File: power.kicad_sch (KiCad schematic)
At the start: 13 parts, among them J601 CONN_12V, J602 Screw_Terminal_01x02, Q601 DMP3037LSS, SW601 PWR_SW, U601 LM2576S-3.3

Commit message: Power switch footprint.
This is the last footprint!
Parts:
- SW601: footprint (none) -> marco-ram-board:SW_CuK_L101xxxMS02x_SPST_Straight; Part (none) -> 611-L101011MS02Q
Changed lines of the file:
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@@
     (property "Reference" "SW601" (id 0) (at 109.22 67.0392 0))
     (property "Value" "PWR_SW" (id 1) (at 109.22 69.5761 0))
-    (property "Footprint" "" (id 2) (at 109.22 72.39 0)
+    (property "Footprint" "marco-ram-board:SW_CuK_L101xxxMS02x_SPST_Straight" (id 2) (at 109.22 72.39 0)
       (effects (font (size 1.27 1.27)) hide)
     )
-    (property "Datasheet" "~" (id 3) (at 109.22 72.39 0)
+    (property "Datasheet" "https://www.ckswitches.com/media/1423/l.pdf" (id 3) (at 109.22 72.39 0)
       (effects (font (size 1.27 1.27)) hide)
     )
+    (property "Part" "611-L101011MS02Q" (id 4) (at 109.22 72.39 0)
+      (effects (font (size 1.27 1.27)) hide)
+    )

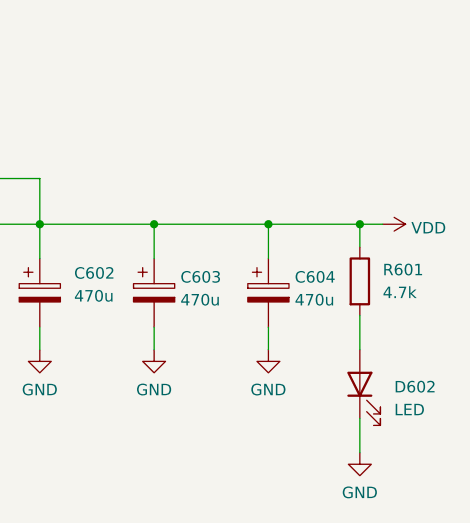
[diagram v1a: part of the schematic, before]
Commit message: Fix led current limiting resistor values.
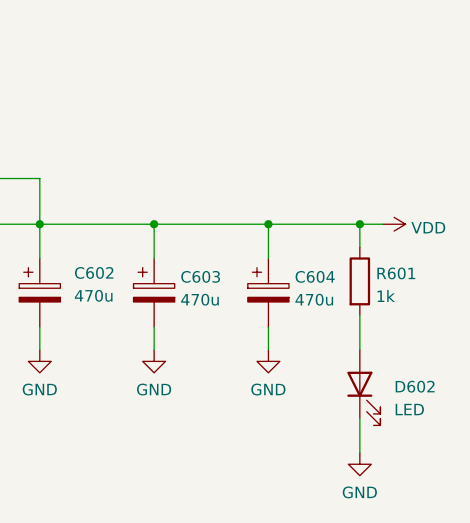
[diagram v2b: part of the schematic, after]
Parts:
- R601: value 4.7k -> 1k
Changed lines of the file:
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@@
   (symbol (lib_id "Device:R") (at 229.87 83.82 0) (unit 1)
     (in_bom yes) (on_board yes) (fields_autoplaced)
-    (property "Reference" "R601" (id 0) (at 232.41 82.5499 0)
+    (property "Reference" "R601" (id 0) (at 231.648 82.9853 0)
       (effects (font (size 1.27 1.27)) (justify left))
     )
-    (property "Value" "4.7k" (id 1) (at 232.41 85.0899 0)
+    (property "Value" "1k" (id 1) (at 231.648 85.5222 0)
       (effects (font (size 1.27 1.27)) (justify left))
     )

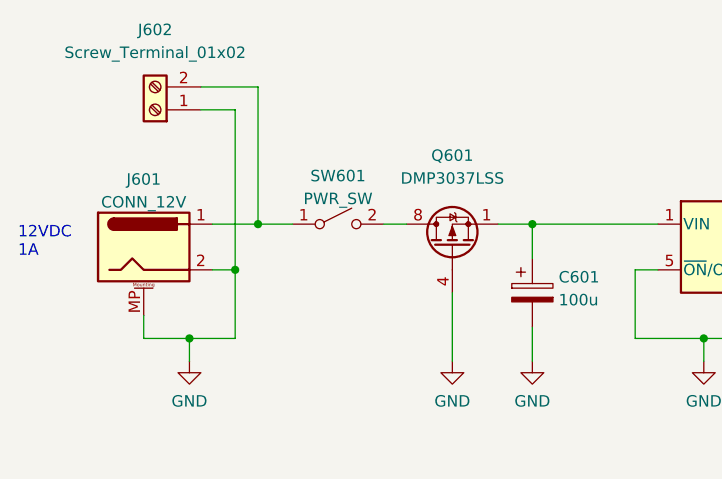
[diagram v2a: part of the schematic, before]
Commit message: Fix several footprints, adjust pcb layout.
- Change footprint for power switch, add the switch's datasheet.
- Rearrange power supply area of PCB to make new switch fit.
- Fix SD card socket footprint to be compatible with the schematic symbol. Add its datasheet
- Add pullups for SD card socket WP and CD (fixed footprint hardwires one side of the switches to GND)
- Add datasheet for the barrel jack.
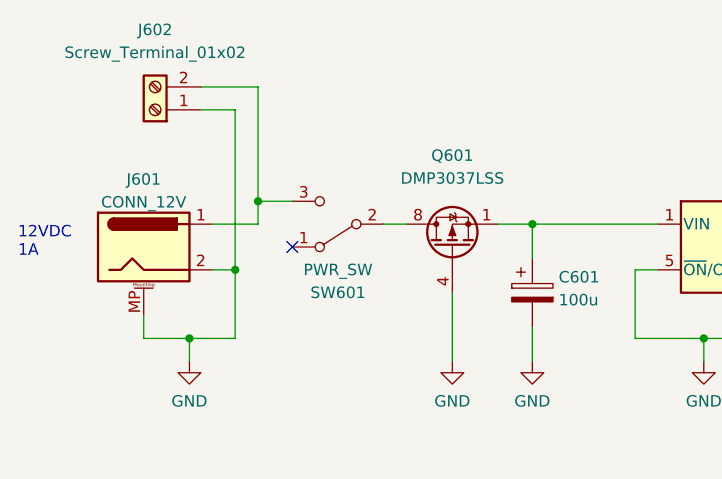
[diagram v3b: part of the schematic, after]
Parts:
- SW601: footprint marco-ram-board:SW_CuK_L101xxxMS02x_SPST_Straight -> marco-ram-board:SW_Slide_CuK_1101M2xxAxx2_SPDT_RightAngle; symbol Switch:SW_SPST -> Switch:SW_SPDT
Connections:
- net at J601.1, J602.2 (Pin_2): now also SW601.3 (C); no longer SW601.1 (A)
- no-connect marks 0 -> 1
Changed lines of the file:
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@@
   (junction (at 176.53 77.47) (diameter 0) (color 0 0 0 0)
   )
-  (junction (at 100.33 72.39) (diameter 0) (color 0 0 0 0)
-  )
   (junction (at 92.71 85.09) (diameter 0) (color 0 0 0 0)
   )
@@
   (junction (at 219.71 77.47) (diameter 0) (color 0 0 0 0)
   )
+  (junction (at 100.33 69.85) (diameter 0) (color 0 0 0 0)
+  )
   (junction (at 229.87 77.47) (diameter 0) (color 0 0 0 0)
   )
   (junction (at 130.81 72.39) (diameter 0) (color 0 0 0 0)
   )
-  (wire (pts (xy 100.33 57.15) (xy 100.33 72.39))
+  (no_connect (at 104.14 74.93))
+  (wire (pts (xy 100.33 57.15) (xy 100.33 69.85))
     (stroke (width 0) (type default) (color 0 0 0 0))
   )
@@
     (stroke (width 0) (type default) (color 0 0 0 0))
   )
+  (wire (pts (xy 100.33 69.85) (xy 100.33 72.39))
+    (stroke (width 0) (type default) (color 0 0 0 0))
+  )
   (wire (pts (xy 176.53 77.47) (xy 176.53 81.28))
     (stroke (width 0) (type default) (color 0 0 0 0))
@@
     (stroke (width 0) (type default) (color 0 0 0 0))
   )
-  (wire (pts (xy 100.33 72.39) (xy 104.14 72.39))
-    (stroke (width 0) (type default) (color 0 0 0 0))
-  )
   (wire (pts (xy 149.86 85.09) (xy 149.86 87.63))
     (stroke (width 0) (type default) (color 0 0 0 0))
@@
   )
   (wire (pts (xy 219.71 88.9) (xy 219.71 91.44))
+    (stroke (width 0) (type default) (color 0 0 0 0))
+  )
+  (wire (pts (xy 100.33 69.85) (xy 104.14 69.85))
     (stroke (width 0) (type default) (color 0 0 0 0))
   )
@@
     (pin "2")
   )
-  (symbol (lib_id "Switch:SW_SPST") (at 109.22 72.39 0) (unit 1)
-    (in_bom yes) (on_board yes) (fields_autoplaced)
-    (property "Reference" "SW601" (id 0) (at 109.22 67.0392 0))
-    (property "Value" "PWR_SW" (id 1) (at 109.22 69.5761 0))
-    (property "Footprint" "marco-ram-board:SW_CuK_L101xxxMS02x_SPST_Straight" (id 2) (at 109.22 72.39 0)
-      (effects (font (size 1.27 1.27)) hide)
-    )
-    (property "Datasheet" "https://www.ckswitches.com/media/1423/l.pdf" (id 3) (at 109.22 72.39 0)
+  (symbol (lib_id "Switch:SW_SPDT") (at 109.22 72.39 180) (unit 1)
+    (in_bom yes) (on_board yes)
+    (property "Reference" "SW601" (id 0) (at 109.22 80.01 0))
+    (property "Value" "PWR_SW" (id 1) (at 109.22 77.4731 0))
+    (property "Footprint" "marco-ram-board:SW_Slide_CuK_1101M2xxAxx2_SPDT_RightAngle" (id 2) (at 109.22 72.39 0)
+      (effects (font (size 1.27 1.27)) hide)
+    )
+    (property "Datasheet" "~" (id 3) (at 109.22 72.39 0)
       (effects (font (size 1.27 1.27)) hide)
     )
@@
     (pin "1")
     (pin "2")
+    (pin "3")
   )
   (symbol (lib_id "Regulator_Switching:LM2576S-3.3") (at 157.48 74.93 0) (unit 1)

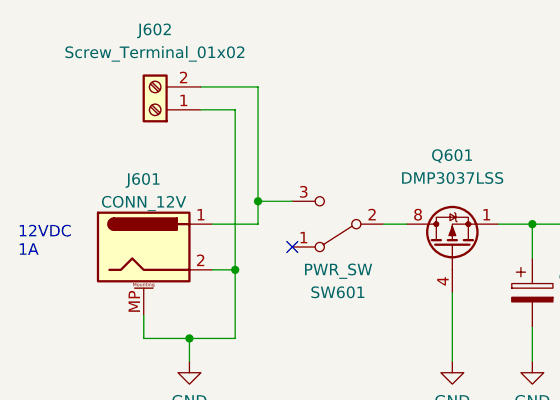
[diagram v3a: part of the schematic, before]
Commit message: Fix overlapped label on DRAM data bus causing D16 and D18 nets to be connected together.
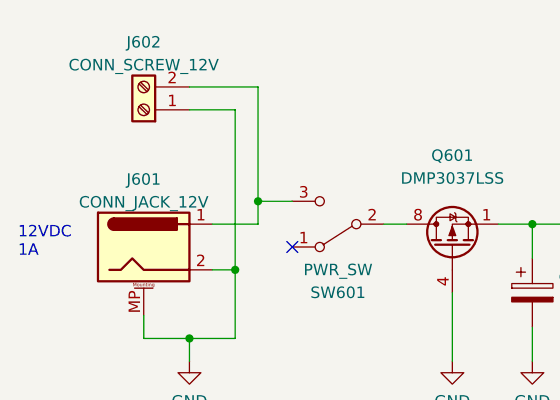
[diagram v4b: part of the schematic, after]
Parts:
- J601: value CONN_12V -> CONN_JACK_12V
- J602: value Screw_Terminal_01x02 -> CONN_SCREW_12V
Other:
- moved on the sheet: J602
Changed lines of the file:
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@@
     (stroke (width 0) (type default) (color 0 0 0 0))
   )
-  (wire (pts (xy 93.98 59.69) (xy 97.79 59.69))
+  (wire (pts (xy 92.71 59.69) (xy 97.79 59.69))
     (stroke (width 0) (type default) (color 0 0 0 0))
   )
@@
     (stroke (width 0) (type default) (color 0 0 0 0))
   )
-  (wire (pts (xy 93.98 57.15) (xy 100.33 57.15))
+  (wire (pts (xy 92.71 57.15) (xy 100.33 57.15))
     (stroke (width 0) (type default) (color 0 0 0 0))
   )
@@
     (pin "2")
   )
-  (symbol (lib_id "Connector:Screw_Terminal_01x02") (at 88.9 59.69 180) (unit 1)
+  (symbol (lib_id "Connector:Screw_Terminal_01x02") (at 87.63 59.69 180) (unit 1)
     (in_bom yes) (on_board yes) (fields_autoplaced)
-    (property "Reference" "J602" (id 0) (at 88.9 50.8 0))
-    (property "Value" "Screw_Terminal_01x02" (id 1) (at 88.9 53.34 0))
-    (property "Footprint" "TerminalBlock_Phoenix:TerminalBlock_Phoenix_MKDS-1,5-2-5.08_1x02_P5.08mm_Horizontal" (id 2) (at 88.9 59.69 0)
+    (property "Reference" "J602" (id 0) (at 87.63 52.1802 0))
+    (property "Value" "CONN_SCREW_12V" (id 1) (at 87.63 54.7171 0))
+    (property "Footprint" "TerminalBlock_Phoenix:TerminalBlock_Phoenix_MKDS-1,5-2-5.08_1x02_P5.08mm_Horizontal" (id 2) (at 87.63 59.69 0)
       (effects (font (size 1.27 1.27)) hide)
     )
-    (property "Datasheet" "~" (id 3) (at 88.9 59.69 0)
+    (property "Datasheet" "~" (id 3) (at 87.63 59.69 0)
       (effects (font (size 1.27 1.27)) hide)
     )
@@
     (in_bom yes) (on_board yes) (fields_autoplaced)
     (property "Reference" "J601" (id 0) (at 87.63 67.4202 0))
-    (property "Value" "CONN_12V" (id 1) (at 87.63 69.9571 0))
+    (property "Value" "CONN_JACK_12V" (id 1) (at 87.63 69.9571 0))
     (property "Footprint" "Connector_BarrelJack:BarrelJack_CUI_PJ-063AH_Horizontal" (id 2) (at 88.9 75.946 0)
       (effects (font (size 1.27 1.27)) hide)

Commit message: Add worksheet template with PoliMi logo.
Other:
- title: (none) -> MARCO RAM Board
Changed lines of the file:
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@@
 (kicad_sch (version 20211123) (generator eeschema)
   (paper "A4")
+  (title_block
+    (title "MARCO RAM Board")
+    (rev "1")
+    (comment 9 "Power Supply")
+  )
   (junction (at 207.01 77.47) (diameter 0) (color 0 0 0 0)
   )

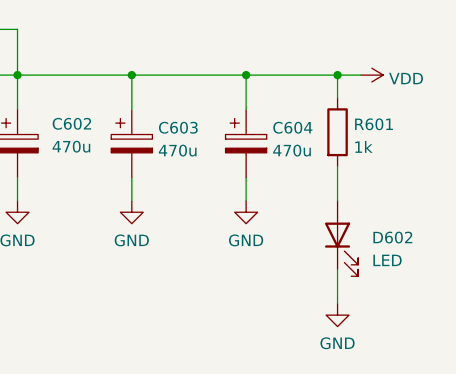
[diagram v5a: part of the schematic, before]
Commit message: Fully update PCB and schematic after BOM consolidation
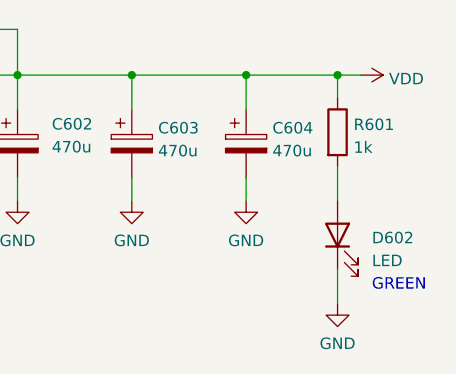
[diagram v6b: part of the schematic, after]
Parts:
- C601: Part 710-860020473008 -> 667-ECA-1EM101I
- C602, C603, C604: Part 667-EEU-FR1C471B -> 667-EEU-EB1A471SB
- D601: Part (none) -> 511-1N5822
- D602: Part (none) -> 327-VCEG1104LSTR
- J602: Part (none) -> 490-TB004-508-02BE
- L601: Part PE-92114KNL -> 673-PE-92114KNL
- Q601: Part (none) -> 621-DMP3037LSS-13
- R601: Part (none) -> 603-RC0603FR-071KL
- SW601: Part 611-L101011MS02Q -> 611-1101M2S3ABE2
- U601: Part (none) -> 926-LM2576SX33NOPB
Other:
- note added: "GREEN"
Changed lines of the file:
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@@
     (effects (font (size 1.27 1.27)) (justify left bottom))
   )
+  (text "GREEN" (at 233.68 101.6 0)
+    (effects (font (size 1.27 1.27)) (justify left bottom))
+  )
   (symbol (lib_id "Device:D_Schottky") (at 176.53 85.09 270) (unit 1)
     (in_bom yes) (on_board yes) (fields_autoplaced)
@@
     )
     (property "Datasheet" "~" (id 3) (at 176.53 85.09 0)
+      (effects (font (size 1.27 1.27)) hide)
+    )
+    (property "Part" "511-1N5822" (id 4) (at 176.53 85.09 0)
       (effects (font (size 1.27 1.27)) hide)
     )
@@
       (effects (font (size 1.27 1.27)) hide)
     )
-    (property "Part" "PE-92114KNL" (id 4) (at 185.42 77.47 90)
+    (property "Part" "673-PE-92114KNL" (id 4) (at 185.42 77.47 90)
       (effects (font (size 1.27 1.27)) hide)
     )
@@
       (effects (font (size 1.27 1.27)) hide)
     )
+    (property "Part" "490-TB004-508-02BE" (id 4) (at 87.63 59.69 0)
+      (effects (font (size 1.27 1.27)) hide)
+    )
     (pin "1")
     (pin "2")
@@
       (effects (font (size 1.27 1.27)) hide)
     )
-    (property "Part" "667-EEU-FR1C471B" (id 4) (at 219.71 85.09 0)
+    (property "Part" "667-EEU-EB1A471SB" (id 4) (at 219.71 85.09 0)
       (effects (font (size 1.27 1.27)) hide)
     )
@@
       (effects (font (size 1.27 1.27)) hide)
     )
-    (property "Part" "710-860020473008" (id 4) (at 130.81 80.01 0)
+    (property "Part" "667-ECA-1EM101I" (id 4) (at 130.81 80.01 0)
       (effects (font (size 1.27 1.27)) hide)
     )
@@
       (effects (font (size 1.27 1.27)) hide)
     )
-    (property "Part" "611-L101011MS02Q" (id 4) (at 109.22 72.39 0)
+    (property "Part" "611-1101M2S3ABE2" (id 4) (at 109.22 72.39 0)
       (effects (font (size 1.27 1.27)) hide)
     )
@@
       (effects (font (size 1.27 1.27)) hide)
     )
+    (property "Part" "926-LM2576SX33NOPB" (id 4) (at 157.48 74.93 0)
+      (effects (font (size 1.27 1.27)) hide)
+    )
     (pin "1")
     (pin "2")
@@
       (effects (font (size 1.27 1.27)) hide)
     )
+    (property "Part" "327-VCEG1104LSTR" (id 4) (at 229.87 95.25 0)
+      (effects (font (size 1.27 1.27)) hide)
+    )
     (pin "1")
     (pin "2")
@@
       (effects (font (size 1.27 1.27)) hide)
     )
+    (property "Part" "603-RC0603FR-071KL" (id 4) (at 229.87 83.82 0)
+      (effects (font (size 1.27 1.27)) hide)
+    )
     (pin "1")
     (pin "2")
@@
       (effects (font (size 1.27 1.27)) hide)
     )
-    (property "Part" "667-EEU-FR1C471B" (id 4) (at 207.01 85.09 0)
+    (property "Part" "667-EEU-EB1A471SB" (id 4) (at 207.01 85.09 0)
       (effects (font (size 1.27 1.27)) hide)
     )
@@
       (effects (font (size 1.27 1.27)) hide)
     )
-    (property "Part" "667-EEU-FR1C471B" (id 4) (at 194.31 85.09 0)
+    (property "Part" "667-EEU-EB1A471SB" (id 4) (at 194.31 85.09 0)
       (effects (font (size 1.27 1.27)) hide)
     )
@@
       (effects (font (size 1.27 1.27)) (justify left) hide)
     )
-    (pin "1")
+    (property "Part" "621-DMP3037LSS-13" (id 4) (at 121.92 74.93 0)
+      (effects (font (size 1.27 1.27)) hide)
+    )
+    (pin "1")

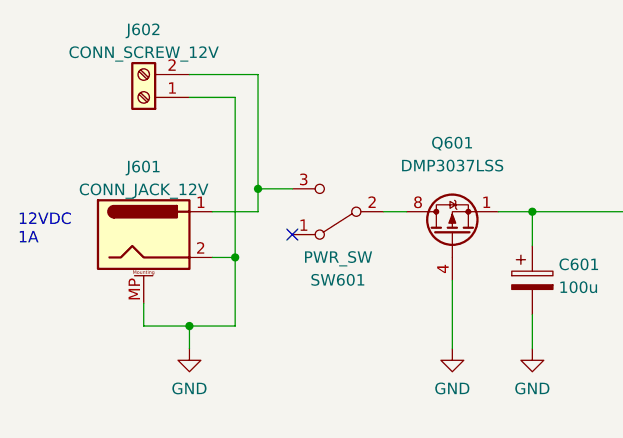
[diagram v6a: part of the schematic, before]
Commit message: Move labels on switches, jumpers and so on to a separate Label property from the Value property.
Value must be the same for components that are physically the same, otherwise it screws up the BOM. But that means we need to add each label manually.
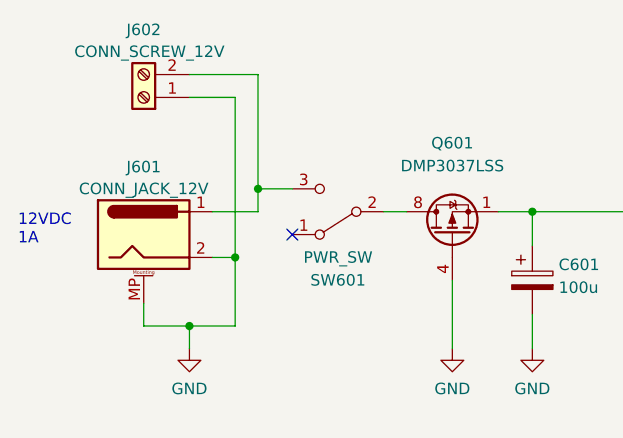
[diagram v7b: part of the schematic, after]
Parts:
- D602: Label (none) -> LED_PWR
- J601: value CONN_JACK_12V -> BarrelJack_CUI_PJ-063AH_Horizontal; Label (none) -> CONN_JACK_12V
- J602: value CONN_SCREW_12V -> TerminalBlock_Phoenix_MKDS-1,5-2-5.08_1x02_P5.08mm_Horizontal; Label (none) -> CONN_SCREW_12V
- SW601: value PWR_SW -> SW_Slide_CuK_1101M2xxAxx2_SPDT_RightAngle; Label (none) -> PWR_SW
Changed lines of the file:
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@@
   )
   (symbol (lib_id "Connector:Screw_Terminal_01x02") (at 87.63 59.69 180) (unit 1)
-    (in_bom yes) (on_board yes) (fields_autoplaced)
+    (in_bom yes) (on_board yes)
     (property "Reference" "J602" (id 0) (at 87.63 52.1802 0))
-    (property "Value" "CONN_SCREW_12V" (id 1) (at 87.63 54.7171 0))
+    (property "Value" "TerminalBlock_Phoenix_MKDS-1,5-2-5.08_1x02_P5.08mm_Horizontal" (id 1) (at 87.63 54.7171 0)
+      (effects (font (size 1.27 1.27)) hide)
+    )
     (property "Footprint" "TerminalBlock_Phoenix:TerminalBlock_Phoenix_MKDS-1,5-2-5.08_1x02_P5.08mm_Horizontal" (id 2) (at 87.63 59.69 0)
       (effects (font (size 1.27 1.27)) hide)
@@
       (effects (font (size 1.27 1.27)) hide)
     )
+    (property "Label" "CONN_SCREW_12V" (id 5) (at 88.265 54.61 0))
     (pin "1")
     (pin "2")
@@
   )
   (symbol (lib_id "Connector:Barrel_Jack_MountingPin") (at 87.63 74.93 0) (unit 1)
-    (in_bom yes) (on_board yes) (fields_autoplaced)
+    (in_bom yes) (on_board yes)
     (property "Reference" "J601" (id 0) (at 87.63 67.4202 0))
-    (property "Value" "CONN_JACK_12V" (id 1) (at 87.63 69.9571 0))
+    (property "Value" "BarrelJack_CUI_PJ-063AH_Horizontal" (id 1) (at 87.63 69.9571 0)
+      (effects (font (size 1.27 1.27)) hide)
+    )
     (property "Footprint" "Connector_BarrelJack:BarrelJack_CUI_PJ-063AH_Horizontal" (id 2) (at 88.9 75.946 0)
       (effects (font (size 1.27 1.27)) hide)
@@
       (effects (font (size 1.27 1.27)) hide)
     )
+    (property "Label" "CONN_JACK_12V" (id 5) (at 87.63 69.85 0))
     (pin "1")
     (pin "2")
@@
     (in_bom yes) (on_board yes)
     (property "Reference" "SW601" (id 0) (at 109.22 80.01 0))
-    (property "Value" "PWR_SW" (id 1) (at 109.22 77.4731 0))
+    (property "Value" "SW_Slide_CuK_1101M2xxAxx2_SPDT_RightAngle" (id 1) (at 109.22 77.4731 0)
+      (effects (font (size 1.27 1.27)) hide)
+    )
     (property "Footprint" "marco-ram-board:SW_Slide_CuK_1101M2xxAxx2_SPDT_RightAngle" (id 2) (at 109.22 72.39 0)
       (effects (font (size 1.27 1.27)) hide)
@@
       (effects (font (size 1.27 1.27)) hide)
     )
+    (property "Label" "PWR_SW" (id 5) (at 109.22 77.47 0))
     (pin "1")
     (pin "2")
@@
       (effects (font (size 1.27 1.27)) hide)
     )
+    (property "Label" "LED_PWR" (id 5) (at 229.87 95.25 0)
+      (effects (font (size 1.27 1.27)) hide)
+    )
